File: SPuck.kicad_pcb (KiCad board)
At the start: 2 copper layers, 10 parts, among them U1 ESP32-S3-WROOM-2, U2 AMS1117-3.3

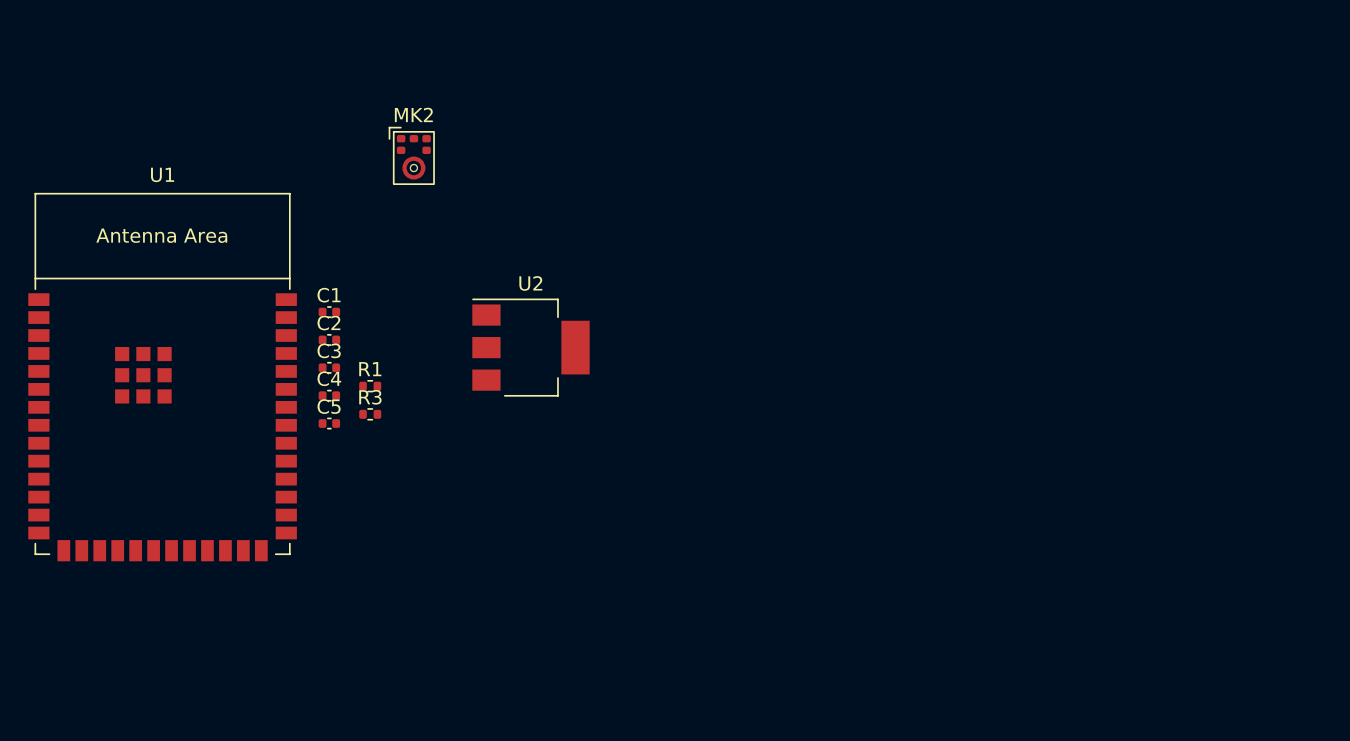
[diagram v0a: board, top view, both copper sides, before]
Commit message: Schematic done, PCB WIP
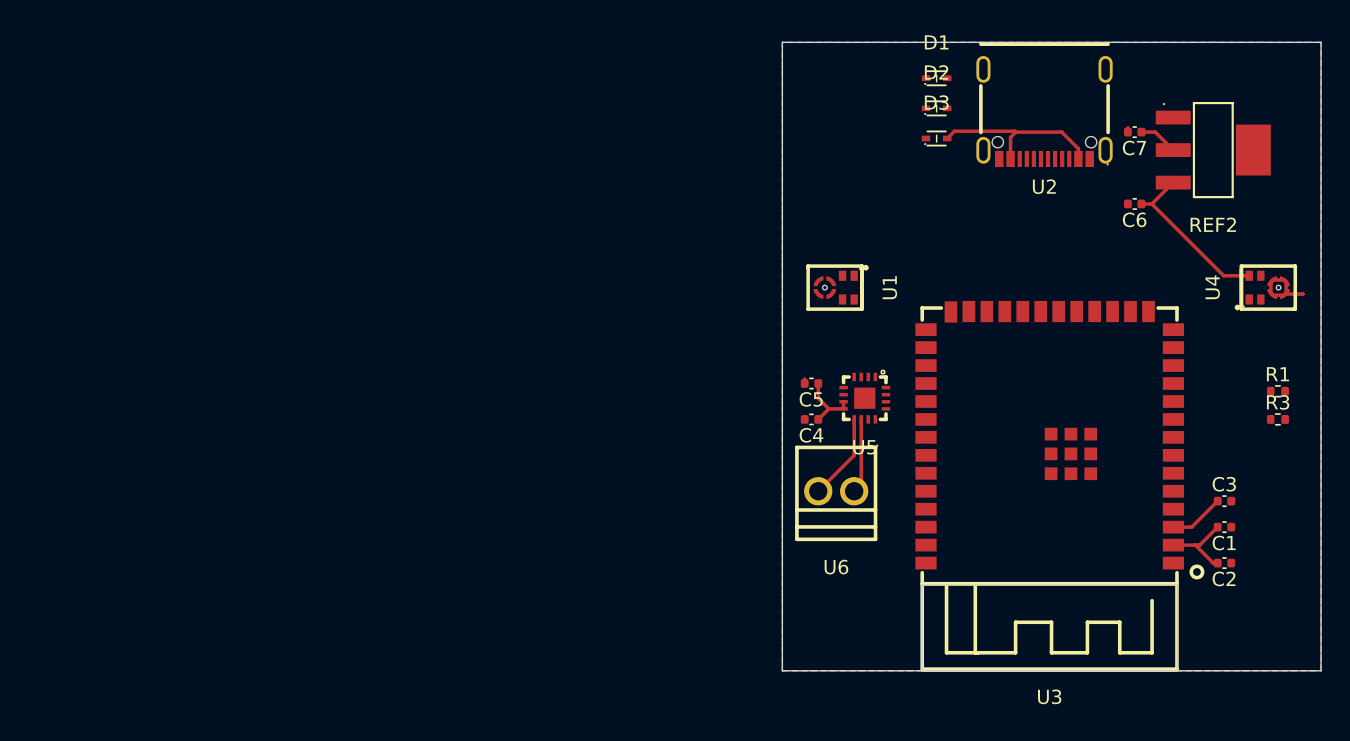
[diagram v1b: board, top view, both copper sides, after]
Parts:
- removed MK2: SPH0645LM4H, Sensor_Audio:Knowles_SPH0645LM4H-6_3.5x2.65mm
- added C6: 10nF, Capacitor_SMD:C_0402_1005Metric, F.Cu at (101.1, 27.9)
- added C7: 10nF, Capacitor_SMD:C_0402_1005Metric, F.Cu at (101.1, 22.9)
- added D1: LESD5D5_0CT1G, footprint:SOD-523_L1.2-W0.8-LS1.6-BI, F.Cu at (87.1, 19.1)
- added D2: LESD5D5_0CT1G, footprint:SOD-523_L1.2-W0.8-LS1.6-BI, F.Cu at (87.1, 21.2)
- added D3: LESD5D5_0CT1G, footprint:SOD-523_L1.2-W0.8-LS1.6-BI, F.Cu at (87.1, 23.3)
- added REF2: AMS1117-3_3_C347222, footprint:SOT-223-4_L6.5-W3.5-P2.30-LS7.0-BR, F.Cu at (106.7, 24.1)
- added U3: ESP32-S3-WROOM-1(N16R8), footprint:WIRELM-SMD_ESP32-S3-WROOM-1, F.Cu at (95.1, 44.4)
- added U4: SD18OB261-060, footprint:MIC-SMD_SD18OB261-060, F.Cu at (110.5, 33.9)
- added U5: MAX98357AETE+T, footprint:TQFN-16_L3.0-W3.0-P0.50-BL-EP1.5, F.Cu at (82.0, 41.7)
- added U6: XY308-2_54-2P, footprint:CONN-TH_XY308-2.54-2P, F.Cu at (80.0, 48.3)
- C4: value 10nF -> 100nF
- C5: value 10nF -> 22nF
- U1: value ESP32-S3-WROOM-2 -> SD18OB261-060; footprint PCM_Espressif:ESP32-S3-WROOM-2 -> footprint:MIC-SMD_SD18OB261-060
- U2: value AMS1117-3.3 -> HC-TYPE-C-16P-CH2_58-3A-02; footprint Package_TO_SOT_SMD:SOT-223-3_TabPin2 -> footprint:USB-C-SMD_HC-TYPE-C-16P-CH3.18-3A-02
- moved C2 65.2 mm to (107.5, 53.3), turned to 180 degrees
- moved C1 65.1 mm to (107.5, 50.8), turned to 180 degrees
- moved R1 64.2 mm to (111.2, 41.2)
- moved R3 64.2 mm to (111.2, 43.2)
- moved C3 64.0 mm to (107.5, 49.0)
- moved U1 48.5 mm to (80.0, 33.9), turned to -90 degrees
- moved U2 39.9 mm to (94.7, 21.6), turned to 180 degrees
- moved C5 34.2 mm to (78.3, 40.6), turned to 180 degrees
- moved C4 34.1 mm to (78.3, 43.2), turned to 180 degrees
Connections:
- C1 pad 1: +3.3V -> GND
- C1 pad 2: GND -> +3.3V
- C2 pad 1: +3.3V -> GND
- C2 pad 2: GND -> +3.3V
- C3 pad 1: Net-(U1-EN) -> Net-(U3-EN)
- C4 pad 1: VBUS -> +3.3V
- R1 pad 2: Net-(U1-EN) -> Net-(U3-EN)
- U1 pad 1: GND -> I2S_IN Data
- U1 pad 3: Net-(U1-EN) -> GND
- U1 pad 4: unconnected-(U1-GPIO4/TOUCH4/ADC1_CH3-Pad4) -> I2S_IN Clock
- U1 pad 5: unconnected-(U1-GPIO5/TOUCH5/ADC1_CH4-Pad5) -> +3.3V
- U2 pad 1: GND -> unconnected-(U2-EH-Pad1)
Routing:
- net +3.3V: track 0.00 -> 22.3 mm
- net VBUS: track 0.00 -> 15.5 mm
- net GND: track 0.00 -> 6.55 mm
- net Net-(U5-OUTP): track 0.00 -> 6.13 mm
- net Net-(U5-OUTN): track 0.00 -> 5.29 mm
- net Net-(U3-EN): track 0.00 -> 3.89 mm
- added copper zone on B.Cu, net GND
- added copper zone on F.Cu, net GND
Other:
- board outline added: 38.1 x 44.5 mm
